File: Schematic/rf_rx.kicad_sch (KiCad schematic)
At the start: 12 parts, among them SW2 TS24CA, U1 ME6217C33M5G, U12 ESP-01F-2M, U13 E28-2G4M27SX

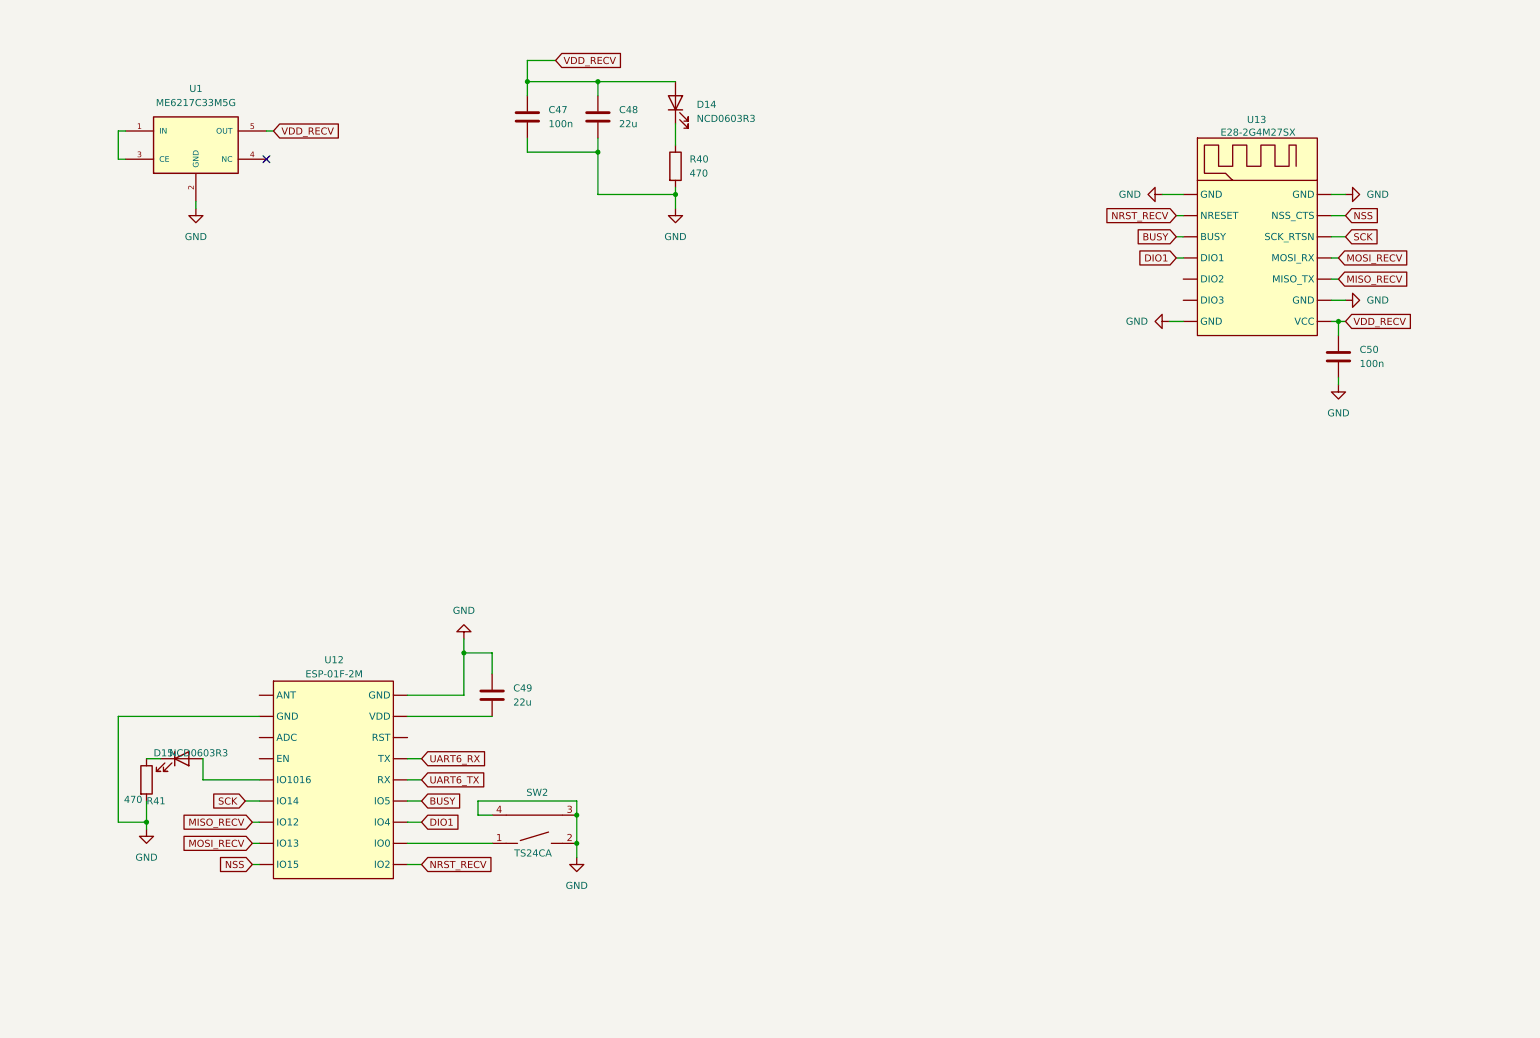
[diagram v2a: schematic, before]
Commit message: Update schematic and footprint libraries with various component modifications
- Updated fp-info-cache with new component details and footprint changes.
- Modified osd.kicad_sch to correct pin types and add no_connect entries.
- Adjusted rf_rx.kicad_sch to fix pin assignments and update component properties.
- Enhanced sensors.kicad_sch with new properties for QMC5883L and SPL06-001 sensors.
- Added new libraries to sym-lib-table and fp-lib-table for better organization and access to components.
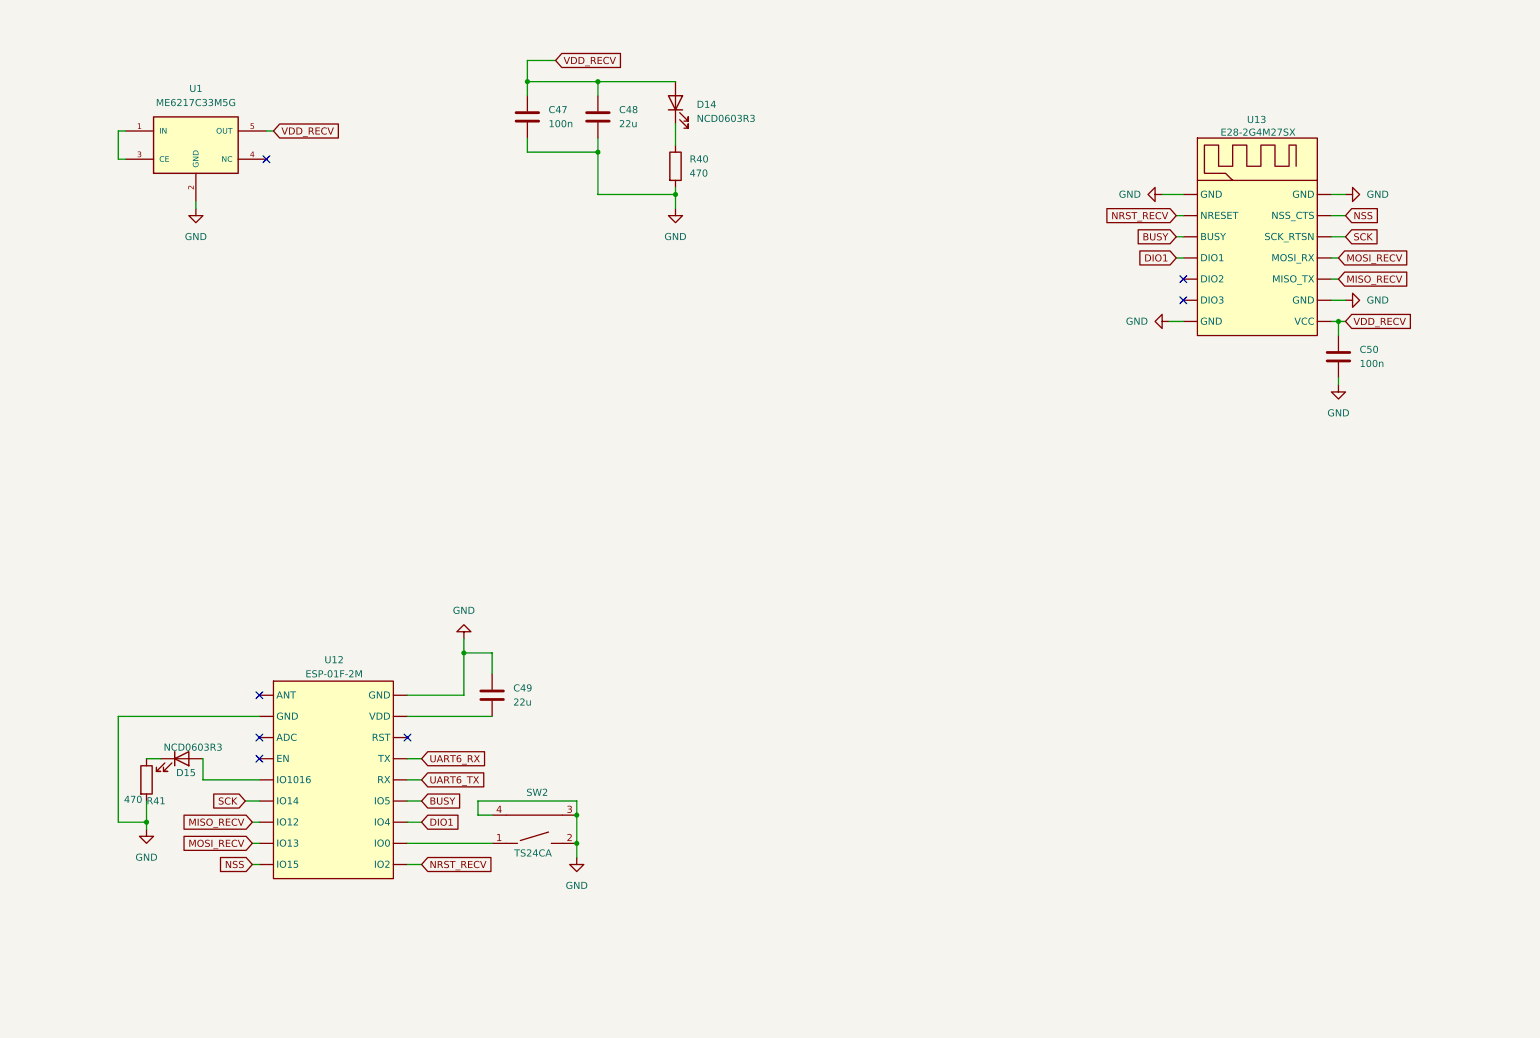
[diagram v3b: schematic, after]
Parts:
- U1: Price (none) -> None
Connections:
- no-connect marks 1 -> 7
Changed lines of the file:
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@@
+	)
+	(no_connect
+		(at 82.55 143.51)
+	)
+	(no_connect
+		(at 55.88 147.32)
 	)
 	(no_connect
 		(at 57.15 39.37)
+	)
+	(no_connect
+		(at 55.88 143.51)
+	)
+	(no_connect
+		(at 55.88 135.89)
+	)
+	(no_connect
+		(at 222.25 60.96)
+	)
+	(no_connect
+		(at 222.25 64.77)
 	)
 	(wire
@@
 			)
 		)
-		(property "Price" ""
+		(property "Price" "None"
 			(at 44.45 36.83 0)
 			(effects
@@
 		(dnp no)
 		(property "Reference" "D15"
-			(at 38.608 146.304 0)
+			(at 42.672 149.86 0)
 			(effects
 				(font
@@
 		)
 		(property "Value" "NCD0603R3"
-			(at 44.958 146.304 0)
+			(at 43.942 145.288 0)
 			(effects
 				(font
@@
 		)
 		(property "Footprint" "fch7_fp:WIFIM-SMD_ESP-01F-2M"
-			(at 69.85 152.4 0)
+			(at 69.342 127.508 0)
 			(effects
 				(font
@@
 		)
 		(property "Datasheet" "https://www.lcsc.com/datasheet/C2764054.pdf"
-			(at 69.85 152.4 0)
+			(at 68.326 172.72 0)
 			(effects
 				(font
@@
 		)
 		(property "MPN" "ESP-01F-2M"
-			(at 69.85 152.4 0)
+			(at 99.568 149.352 0)
 			(effects
 				(font
@@
 		)
 		(property "Manufacturer" "Ai-Thinker"
-			(at 69.85 152.4 0)
-			(effects
-				(font
+			(at 109.22 159.766 0)
+			(effects
+				(font

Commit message: Refactor fp-lib-table: Remove unused libraries and update description for fch7_fp
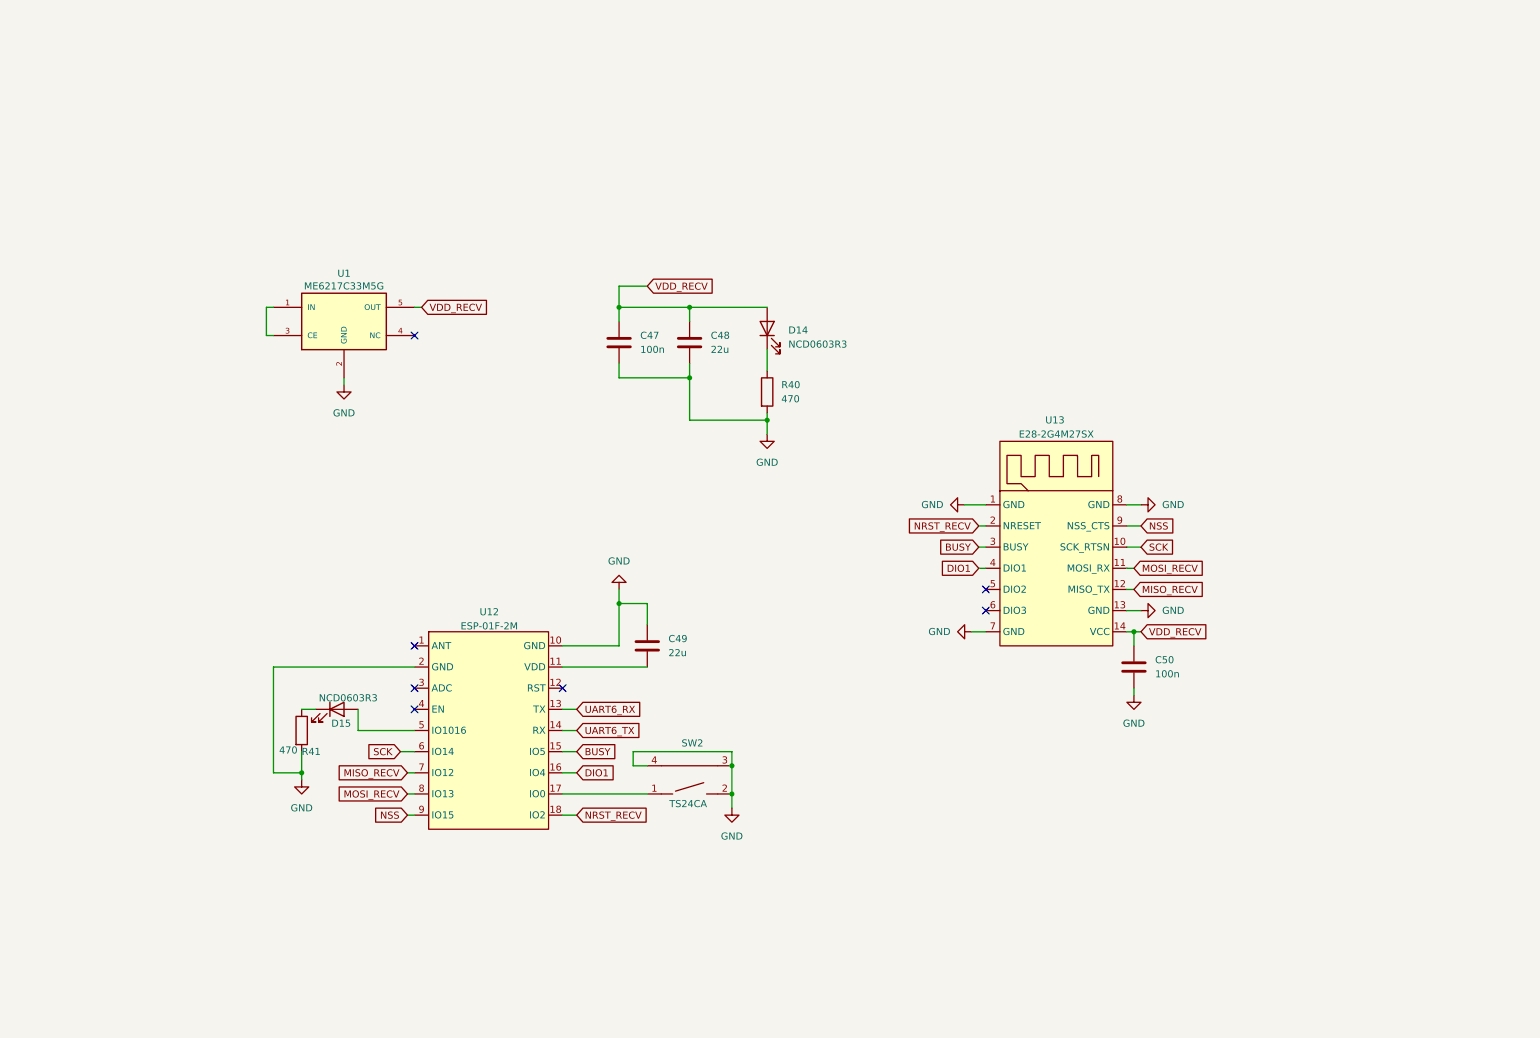
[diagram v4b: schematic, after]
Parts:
- SW2: footprint ProLib_pcs_2025-11-24:SW-SMD_2P-TS24CA -> fch7_fp:SW-SMD_2P-TS24CA
- U1: footprint ME6217C33M5G:SOT23-5 -> fch7_fp:SOT23-5
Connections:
- net BUSY: now also U12.15 (IO5), U13.3 (BUSY); no longer U12. (IO2), U13. (VCC)
- net DIO1: now also U12.16 (IO4), U13.4 (DIO1); no longer U12. (IO2), U13. (VCC)
- net GND: now also U12.10 (GND), U12.2 (GND), U13.1 (GND), U13.13 (GND), U13.7 (GND), U13.8 (GND); no longer U12. (IO2), U13. (VCC)
- net MISO_RECV: now also U12.7 (IO12), U13.12 (MISO_TX); no longer U12. (IO2), U13. (VCC)
- net MOSI_RECV: now also U12.8 (IO13), U13.11 (MOSI_RX); no longer U12. (IO2), U13. (VCC)
- net NRST_RECV: now also U12.18 (IO2), U13.2 (NRESET); no longer U12. (IO2), U13. (VCC)
- net NSS: now also U12.9 (IO15), U13.9 (NSS_CTS); no longer U12. (IO2), U13. (VCC)
- net SCK: now also U12.6 (IO14), U13.10 (SCK_RTSN); no longer U12. (IO2), U13. (VCC)
- net UART6_RX: now also U12.13 (TX); no longer U12. (IO2)
- net UART6_TX: now also U12.14 (RX); no longer U12. (IO2)
- net VDD_RECV: now also U13.14 (VCC); no longer U13. (VCC)
- net at D15.2 (A): now also U12.5 (IO1016); no longer U12. (IO2)
- net at SW2.1: now also U12.17 (IO0); no longer U12. (IO2)
- net at C49.2: now also U12.11 (VDD); no longer U12. (IO2)
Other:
- moved on the sheet: C47, C48, C49, C50, D14, D15, R40, R41, SW2, U1
